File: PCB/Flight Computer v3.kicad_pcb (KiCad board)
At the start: 6 copper layers, 30 x 60 mm, 101 parts, among them J601 USB_C_Receptacle_USB2.0_16P, J602 Conn_02x07_Counter_Clockwise, J603 Screw_Terminal_01x08, J604 Conn_01x02_Pin, J605 Conn_01x05, J701 Conn_Coaxial, U201 LM1117MP-3.3, U301 MMC5633NJL, U302 LSM6DSV320, U303 MS5607-02BA, U304 SAM-M8Q, U401 UT6MA3TCR, U402 UT6MA3TCR, U403 UT6MA3TCR, U501 W25Q128JVS, U502 STM32F446RETx, U701 SX1262, U702 SKY13453-385LF, Y501 25MHz, Y701 NX2016SA-32MHZ-STD-CZS-5

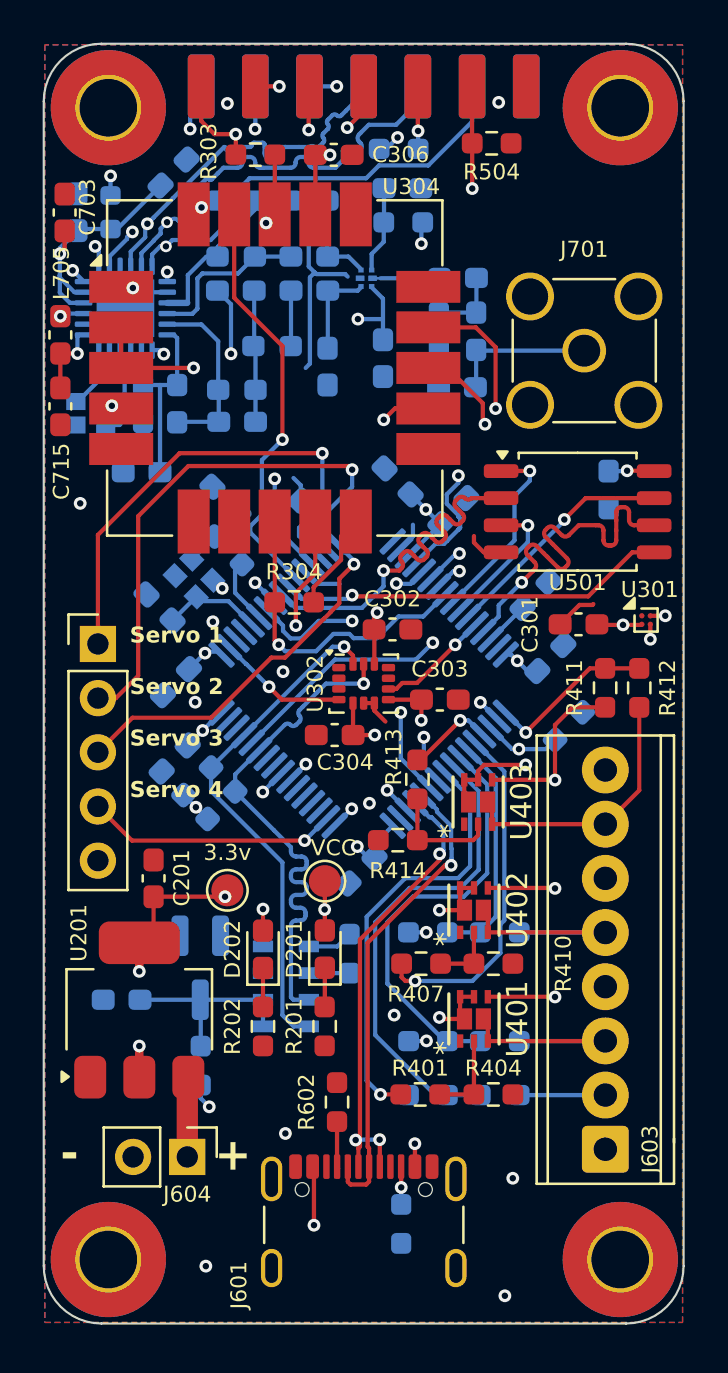
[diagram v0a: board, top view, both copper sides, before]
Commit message: Fixed small PCB problems, and setup build env
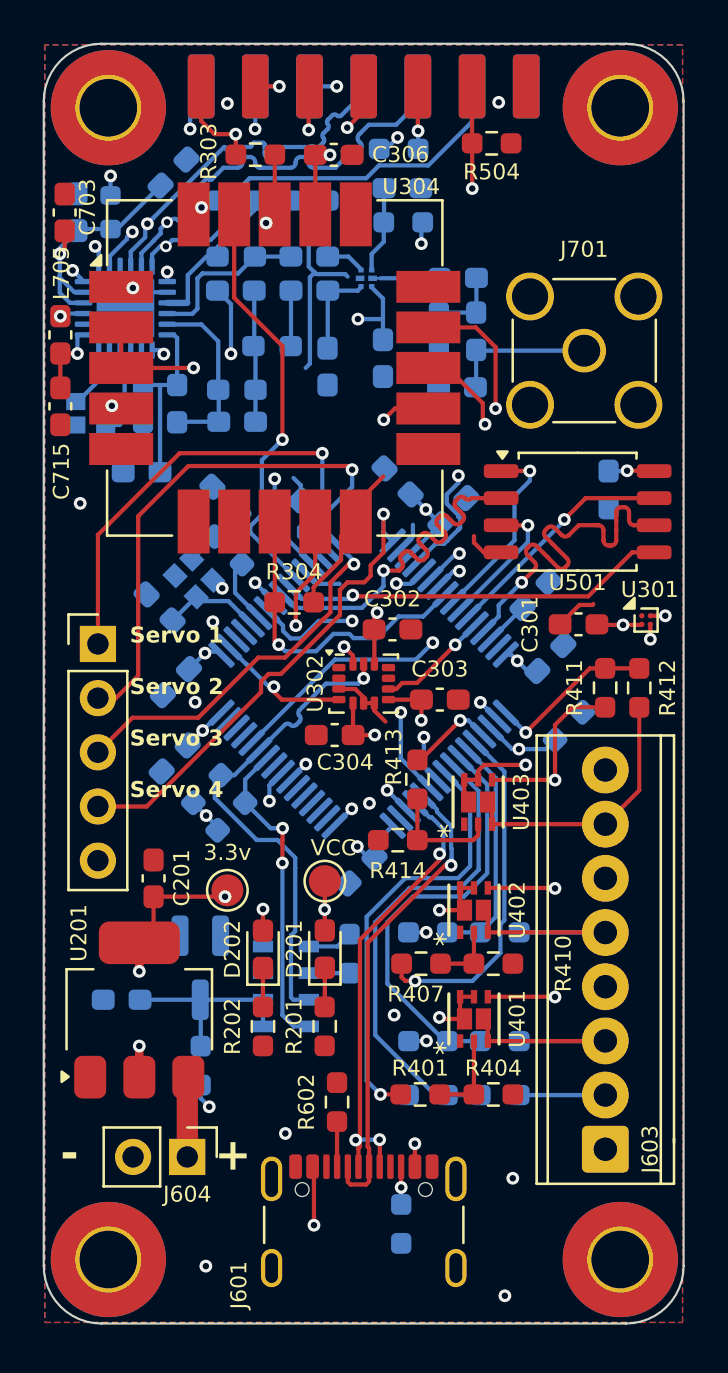
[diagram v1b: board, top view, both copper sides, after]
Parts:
- moved R501 2.30 mm to (106.5, 88.7)
- moved R502 1.01 mm to (105.3, 87.4)
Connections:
- U502 pad 17: unconnected-(U502-PA3-Pad17) -> Servo4
- U502 pad 50: Servo4 -> unconnected-(U502-PA15-Pad50)
- U502 pad 58: unconnected-(U502-PB6-Pad58) -> I2C_SCL
- U502 pad 61: I2C_SCL -> unconnected-(U502-PB8-Pad61)
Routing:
- net Servo4: track 11.8 -> 22.9 mm
- net GND: track 31.7 -> 35.9 mm, vias 17 -> 16
- net I2C_SCL: track 81.9 -> 83.6 mm, vias 4 -> 6
- net I2C_SDA: track 83.0 -> 82.0 mm
- net LORA_BUSY: track 36.0 -> 36.9 mm

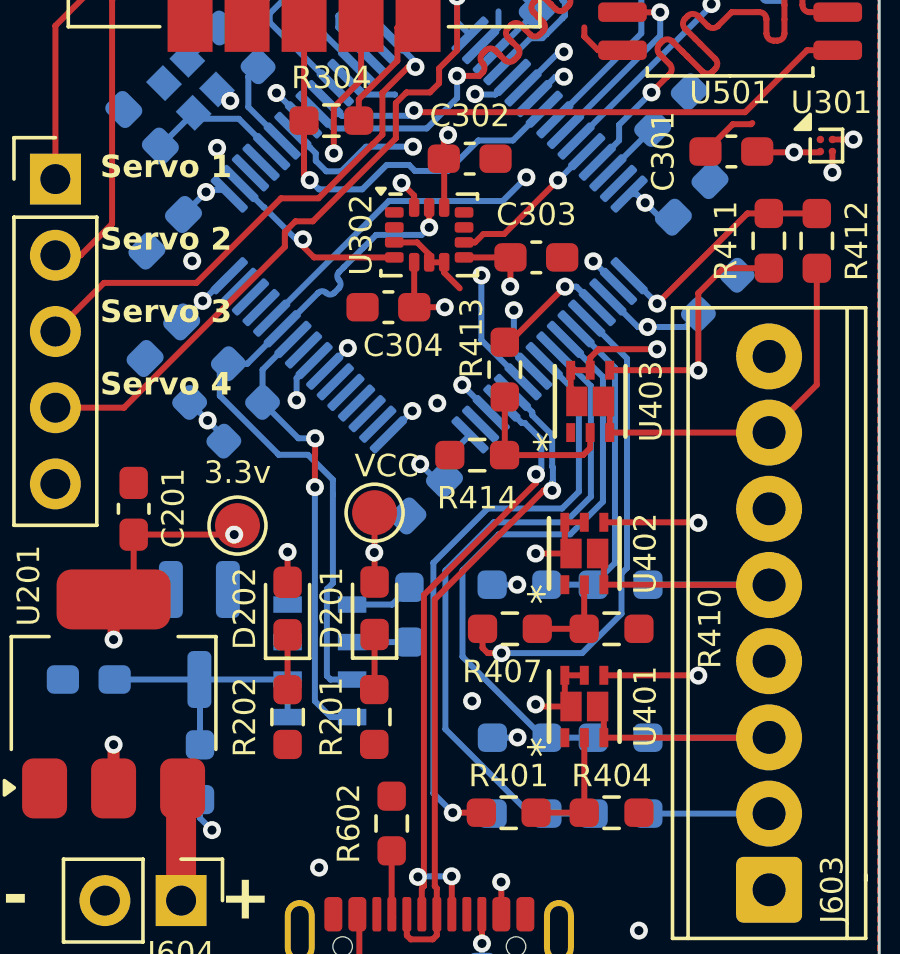
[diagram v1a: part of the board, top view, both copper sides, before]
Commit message: Moved i2c to different set of pins
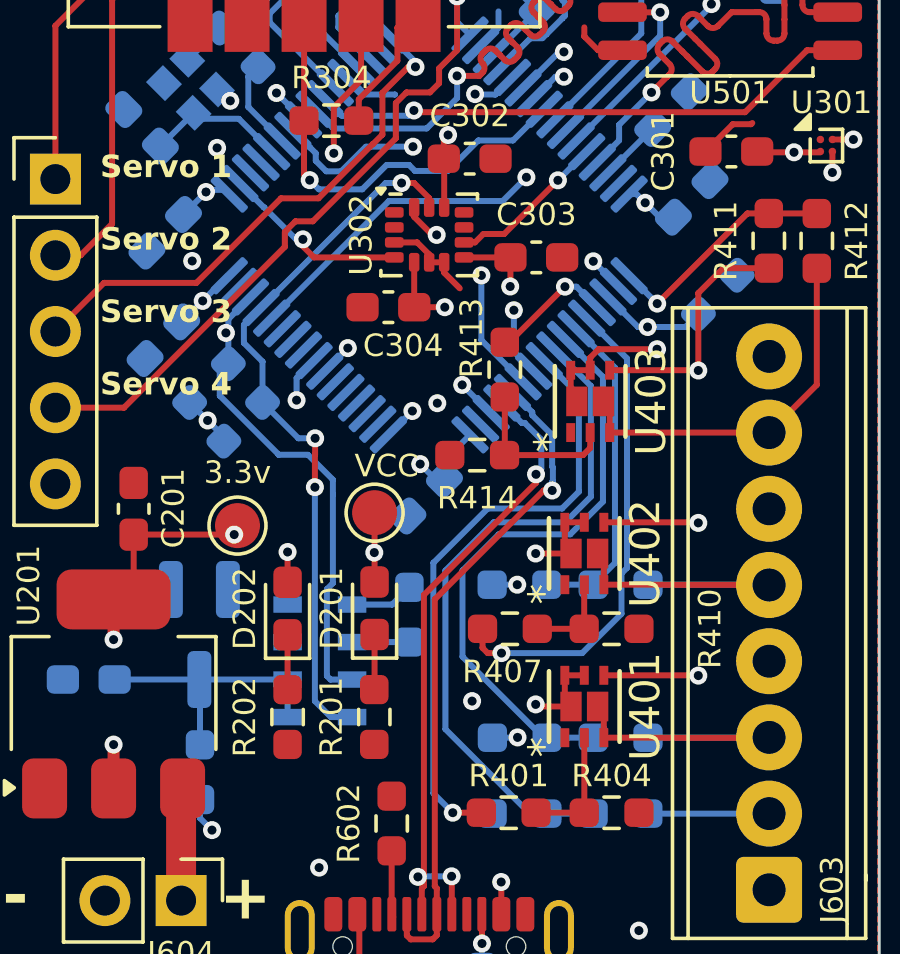
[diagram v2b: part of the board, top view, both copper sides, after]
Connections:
- U302 pad 13: I2C_SDA -> I2C_SCL
- U302 pad 14: I2C_SCL -> I2C_SDA
- U502 pad 58: I2C_SCL -> unconnected-(U502-PB6-Pad58)
- U502 pad 59: I2C_SDA -> unconnected-(U502-PB7-Pad59)
- U502 pad 61: unconnected-(U502-PB8-Pad61) -> I2C_SCL
- U502 pad 62: unconnected-(U502-PB9-Pad62) -> I2C_SDA
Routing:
- net I2C_SCL: track 83.6 -> 91.6 mm
- net I2C_SDA: track 82.0 -> 83.8 mm, vias 4 -> 5

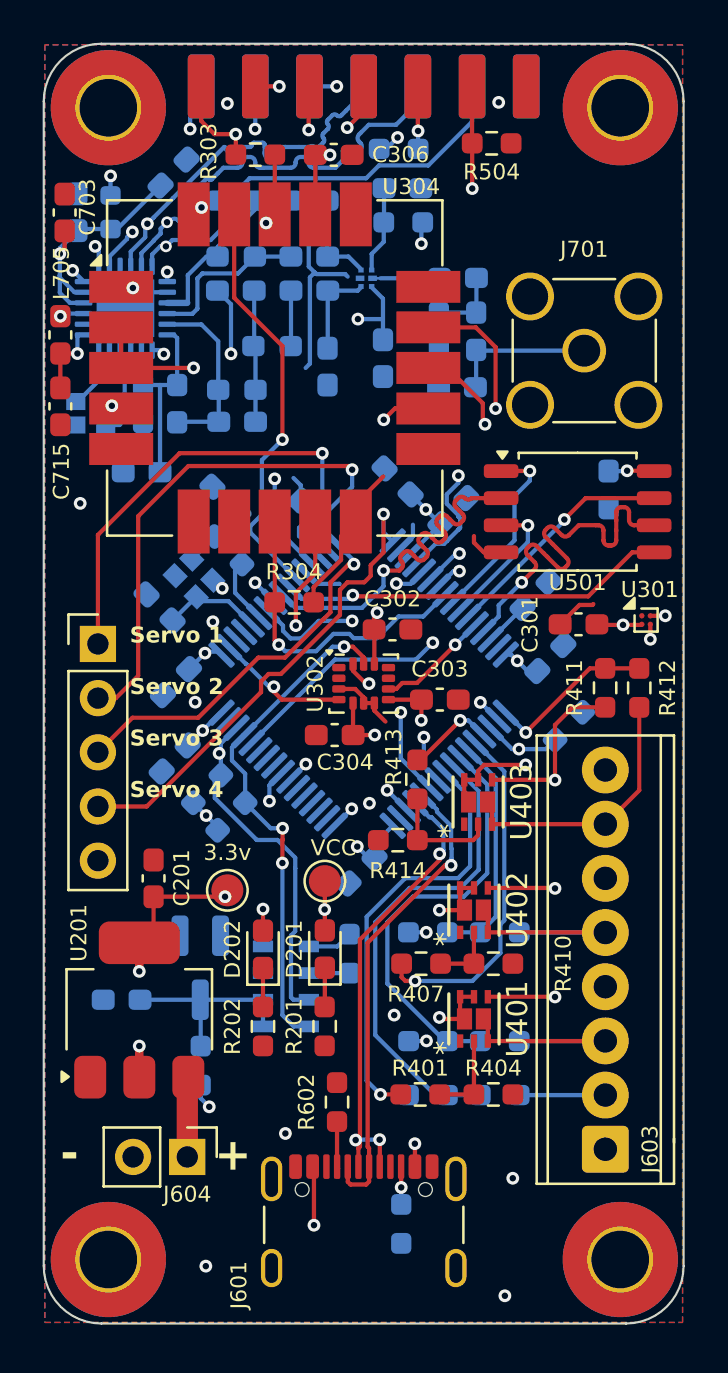
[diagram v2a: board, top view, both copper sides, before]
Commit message: Made sensors use SPI instead of I2C Change external I2C connector to qwiic Made SWD have its own pin header
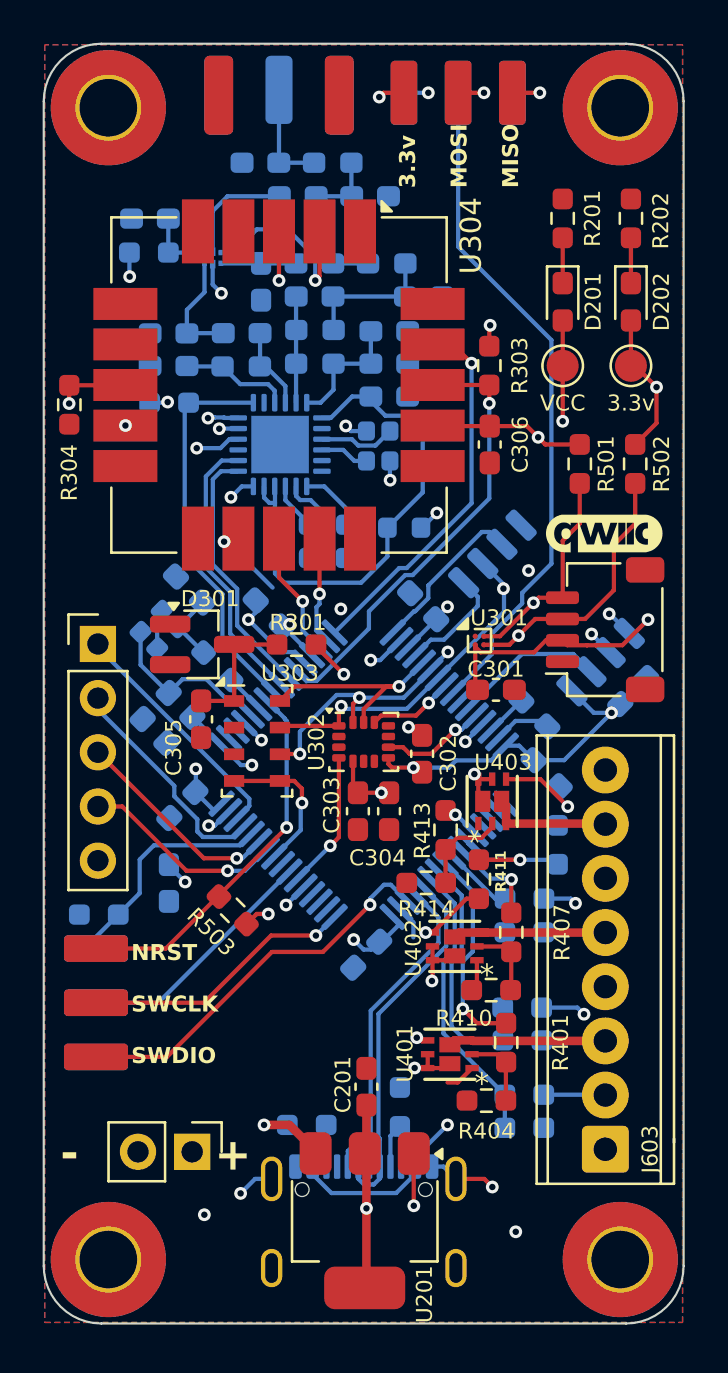
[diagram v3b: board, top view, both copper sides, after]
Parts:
- removed R302: 10k, Resistor_SMD:R_0603_1608Metric_Pad0.98x0.95mm_HandSolder
- added G601: qwiic_Logo, imported:qwiic_5.5mm, F.Cu at (124.0, 75.5)
- added J606: Conn_02x03_Counter_Clockwise, imported:EdgePinHeader_02x03, F.Cu at (114.6, 54.8)
- added J607: Conn_01x04, Connector_JST:JST_SH_SM04B-SRSS-TB_1x04-1MP_P1.00mm_Horizontal, F.Cu at (124.0, 80.0)
- C305, D301, R301, R501, R502, R503, U303: moved to F.Cu
- C703, C715, J601, L705, R412, R504, R602, U501: moved to B.Cu
- J602: value Conn_02x07_Counter_Clockwise -> Conn_02x03_Counter_Clockwise; footprint imported:EdgePinHeader_02x07 -> imported:EdgePinHeader_02x03
- J701: footprint Connector_Coaxial:SMA_Amphenol_132134-11_Vertical -> Connector_Coaxial:SMA_Samtec_SMA-J-P-H-ST-EM1_EdgeMount; moved to B.Cu
- moved R202 41.6 mm to (125.2, 60.7), turned to -90 degrees
- moved J602 40.7 mm to (100.1, 94.9), turned to -90 degrees
- moved R504 40.6 mm to (100.3, 93.3), turned to 180 degrees
- moved R201 39.5 mm to (122.0, 60.7), turned to -90 degrees
- moved R503 36.5 mm to (106.5, 93.1), turned to 135 degrees
- moved D202 34.9 mm to (125.2, 64.6), turned to -90 degrees
- moved D201 32.3 mm to (122.0, 64.6), turned to -90 degrees
- moved TP202 31.0 mm to (125.2, 67.6)
- moved TP201 26.6 mm to (122.0, 67.6)
- moved R502 25.2 mm to (125.4, 72.2), turned to -90 degrees
- moved R702 24.1 mm to (103.5, 69.3), turned to 0 degrees
- moved R501 23.2 mm to (122.8, 72.2), turned to -90 degrees
- moved C503 21.7 mm to (103.5, 91.8), turned to -90 degrees
- moved C502 21.2 mm to (112.8, 95.2), turned to -135 degrees
- moved R301 20.2 mm to (109.5, 80.7), turned to 180 degrees
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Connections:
- J602 pad 1: +3.3V -> NRST
- J602 pad 2: SWO -> SWCLK
- J602 pad 3: SWCLK -> SWDIO
- J602 pad 4: SWDIO -> GND
- J602 pad 5: NRST -> SWO
- R702 pad 1: +3V3 -> +3.3V
- U302 pad 1: GND -> SPI_MOSI
- U302 pad 12: +3.3V -> IMU_CS
- U302 pad 13: I2C_SCL -> SPI_SCK
- U302 pad 14: I2C_SDA -> SPI_MISO
- U303 pad 2: +3V -> GND
- U303 pad 4: GND -> Baro_CS
- U303 pad 5: GND -> Baro_CS
- U303 pad 6: Net-(U303-SDO) -> SPI_MISO
- U303 pad 7: I2C_SDA -> SPI_MOSI
- U303 pad 8: I2C_SCL -> SPI_SCK
- U501 pad 2: /MCU/FLASH_MOSI -> SPI_MOSI
- U501 pad 5: /MCU/FLASH_MISO -> SPI_MISO
- U501 pad 6: /MCU/FLASH_CLK -> SPI_SCK
- U502 pad 10: /MCU/FLASH_MISO -> LORA_DIO1
- U502 pad 11: GPS_INT -> /GPS_RESET
- U502 pad 14: Servo1 -> GPS_TX
- U502 pad 15: Servo2 -> GPS_RX
- U502 pad 16: Servo3 -> GPS_INT
- U502 pad 17: Servo4 -> /MCU//FLASH_WP
- U502 pad 2: IMU_INT1 -> unconnected-(U502-PC13-Pad2)
- U502 pad 20: SPI_CS1 -> /MCU/FLASH_CS
- U502 pad 24: /GPS_SAFEBOOT -> IMU_CS
- U502 pad 25: /MCU/FLASH_CS -> SPI_CS1
- U502 pad 26: /MCU//FLASH_WP -> unconnected-(U502-PB0-Pad26)
- U502 pad 29: /MCU/FLASH_CLK -> I2C_SCL
- U502 pad 33: Pyro3_Cont -> unconnected-(U502-PB12-Pad33)
- U502 pad 34: LORA_DIO1 -> unconnected-(U502-PB13-Pad34)
- U502 pad 35: LORA_SEL -> unconnected-(U502-PB14-Pad35)
- U502 pad 36: Pyro3_Trigger -> unconnected-(U502-PB15-Pad36)
- U502 pad 37: Pyro2_Trigger -> Pyro3_Trigger
- U502 pad 38: Pyro2_Cont -> Pyro3_Cont
- U502 pad 39: Pyro1_Cont -> Pyro2_Trigger
- U502 pad 4: unconnected-(U502-PC15-Pad4) -> /GPS_SAFEBOOT
- U502 pad 40: Armed -> Pyro2_Cont
- U502 pad 42: GPS_RX -> Pyro1_Cont
- U502 pad 43: GPS_TX -> Armed
- U502 pad 53: unconnected-(U502-PC12-Pad53) -> I2C_SDA
- U502 pad 54: unconnected-(U502-PD2-Pad54) -> IMU_INT1
- U502 pad 56: LORA_BUSY -> unconnected-(U502-PB4-Pad56)
- U502 pad 57: unconnected-(U502-PB5-Pad57) -> Baro_CS
- U502 pad 58: unconnected-(U502-PB6-Pad58) -> Servo4
- U502 pad 59: unconnected-(U502-PB7-Pad59) -> Servo3
- U502 pad 61: I2C_SCL -> Servo2
- U502 pad 62: I2C_SDA -> Servo1
- U502 pad 8: /GPS_RESET -> LORA_SEL
- U502 pad 9: /MCU/FLASH_MOSI -> LORA_BUSY
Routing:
- net I2C_SCL: track 91.6 -> 34.9 mm, vias 6 -> 3
- net I2C_SDA: track 83.8 -> 56.7 mm, vias 5 -> 3
- net BOOT0: track 37.3 -> 10.8 mm, vias 2 -> 0
- net LORA_DIO1: track 38.0 -> 12.1 mm, vias 2 -> 0
- net +3.3V: track 61.9 -> 87.0 mm, vias 23 -> 21
- net SWO: track 35.8 -> 11.6 mm, vias 2 -> 0
- net SPI_SCK: track 45.7 -> 69.6 mm, vias 2 -> 4
- net LORA_BUSY: track 36.9 -> 13.1 mm, vias 2 -> 0
- net SWCLK: track 35.9 -> 12.9 mm, vias 2 -> 1
- net GPS_RX: track 25.6 -> 5.03 mm, vias 2 -> 1
- net SPI_MISO: track 45.6 -> 65.7 mm, vias 2 -> 6
- net /MCU/FLASH_MISO: track 18.3 -> 0.00 mm, vias 1 -> 0
- net /MCU/FLASH_CLK: track 18.1 -> 0.00 mm, vias 1 -> 0
- net SWDIO: track 36.4 -> 18.5 mm, vias 2 -> 1
- net LORA_SEL: track 36.4 -> 18.5 mm, vias 2 -> 0
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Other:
- board text added: "3.3v MOSI MISO"
- board text added: "BOOT SWO GND"
- board text added: "GND CS SCK"
- board text added: "NRST SWCLK SWDIO"
- board text removed: "Servo 1 Servo 2 Servo 3 Servo 4"
